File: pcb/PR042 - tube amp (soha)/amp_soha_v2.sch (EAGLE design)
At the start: 55 parts, among them IC1 NE5535U, IC2 7812, IC3 7912, Q1 J113, Q2 J113, Q3 J113, Q4 J113

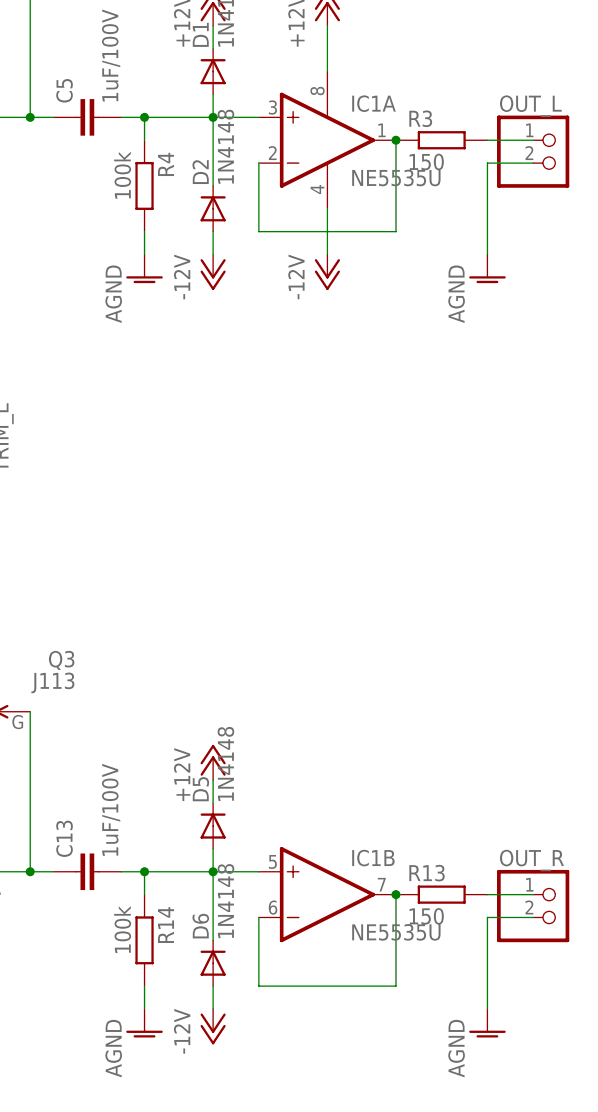
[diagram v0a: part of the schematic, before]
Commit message: 
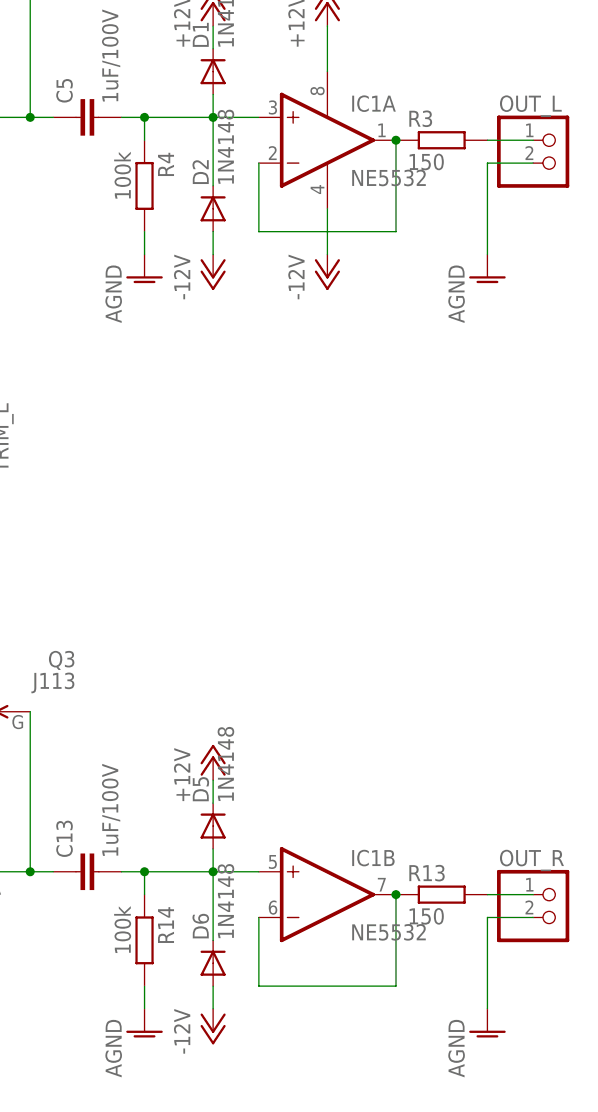
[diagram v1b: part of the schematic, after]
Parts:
- IC1: value NE5535U -> NE5532
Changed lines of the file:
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@@
 <?xml version="1.0" encoding="utf-8"?>
 <!DOCTYPE eagle SYSTEM "eagle.dtd">
-<eagle version="6.4">
+<eagle version="6.5.0">
 <drawing>
 <settings>
@@
 <part name="C5" library="amp_soha" deviceset="C-EU" device="075-052X106" value="1uF/100V"/>
 <part name="P+3" library="amp_soha" deviceset="+24V" device=""/>
-<part name="IC1" library="amp_soha" deviceset="NE5535" device="U"/>
+<part name="IC1" library="amp_soha" deviceset="NE5535" device="U" value="NE5532"/>
 <part name="P-2" library="amp_soha" deviceset="-12V" device=""/>
 <part name="P+4" library="amp_soha" deviceset="+12V" device=""/>
